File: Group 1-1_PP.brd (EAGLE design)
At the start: 90 x 75 mm, 40 parts, among them IC1 74LS90N, IC10 7805T, IC2 74LS90N, IC3 74LS48N, IC4 74LS48N, IC5 74ALS08N, IC6 LM555N, IC7 74LS14N, IC8 7476N, IC9 74LS32N

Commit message: MANAAAAAAAAAAAAAAAAAAAA
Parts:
- moved C5 146.4 mm to (77.0, 18.7)
- moved C3 144.2 mm to (82.5, 23.7)
- moved C2 131.8 mm to (77.0, 23.7)
- moved IC9 130.4 mm to (60.0, 9.00)
- moved C1 112.7 mm to (82.0, 18.6)
- moved IC7 107.5 mm to (63.0, 34.0)
- moved IC6 105.5 mm to (80.0, 34.0)
- moved IC2 100.7 mm to (30.0, 9.00)
- moved R11 92.7 mm to (21.9, 52.3)
- moved IC5 89.0 mm to (61.0, 21.0)
- moved R19 88.4 mm to (10.9, 3.13)
- moved R10 83.6 mm to (21.9, 49.3)
- moved R17 80.2 mm to (10.8, 66.3)
- moved R16 79.7 mm to (20.9, 69.3)
- moved R5 78.1 mm to (9.85, 55.3)
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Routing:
- net VCC: track 0.00 -> 316.4 mm
- net N$4: track 0.00 -> 138.4 mm
- net N$14: track 0.00 -> 121.5 mm
- net TR: track 0.00 -> 108.5 mm
- net N$3: track 0.00 -> 96.2 mm
- net N$7: track 0.00 -> 87.6 mm
- net CLK_1HZ: track 0.00 -> 84.8 mm
- net N$21: track 0.00 -> 79.5 mm
- net N$23: track 0.00 -> 70.8 mm
- net N$22: track 0.00 -> 69.7 mm
- net RESET: track 0.00 -> 57.9 mm
- net N$5: track 0.00 -> 57.0 mm
- net STRST: track 0.00 -> 56.5 mm
- net N$30: track 0.00 -> 56.0 mm
- net N$1: track 0.00 -> 51.3 mm
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- added copper zone on layer 1, net GND
- added copper zone on layer 16, net GND
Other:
- board text added: "60-second Timer Circuit Rev 1.0"
- board text added: "RESET"
- board text added: "START/STOP"

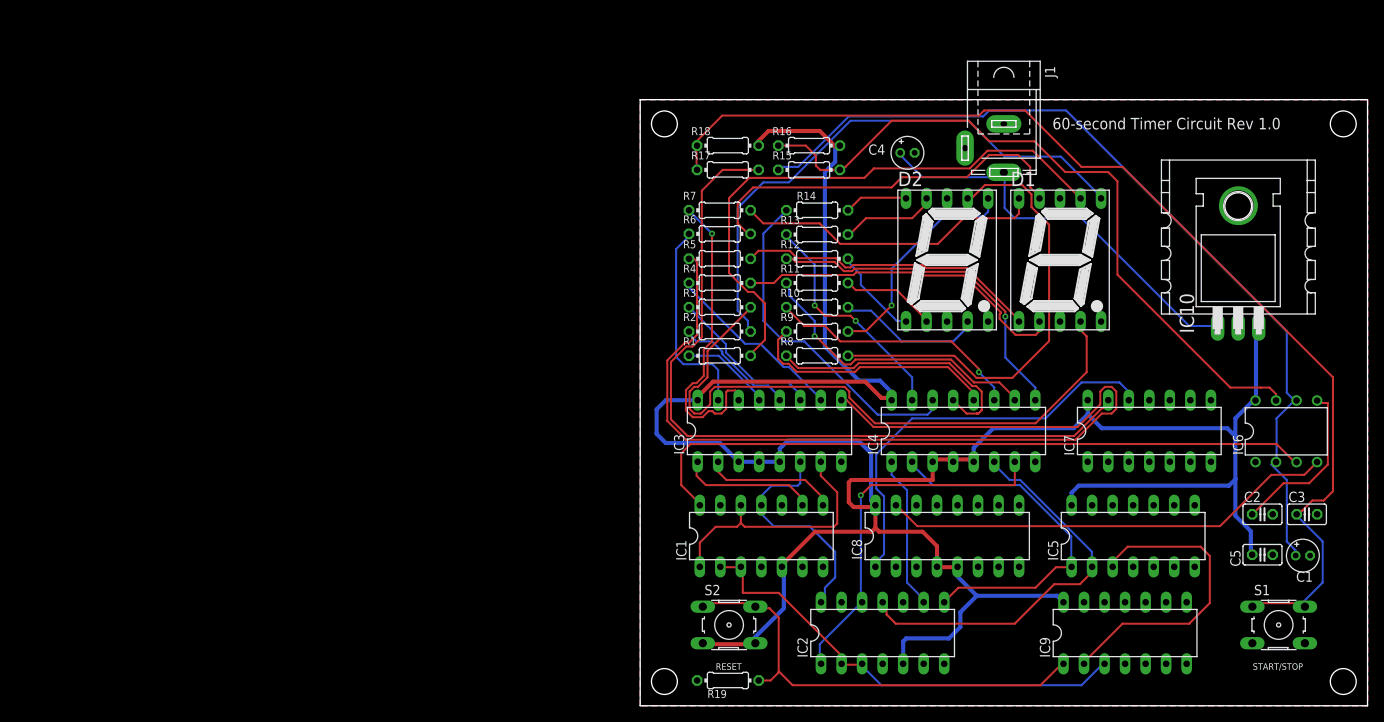
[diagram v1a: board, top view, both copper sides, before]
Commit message: [Zach] Updated lbrs for regulator visibility
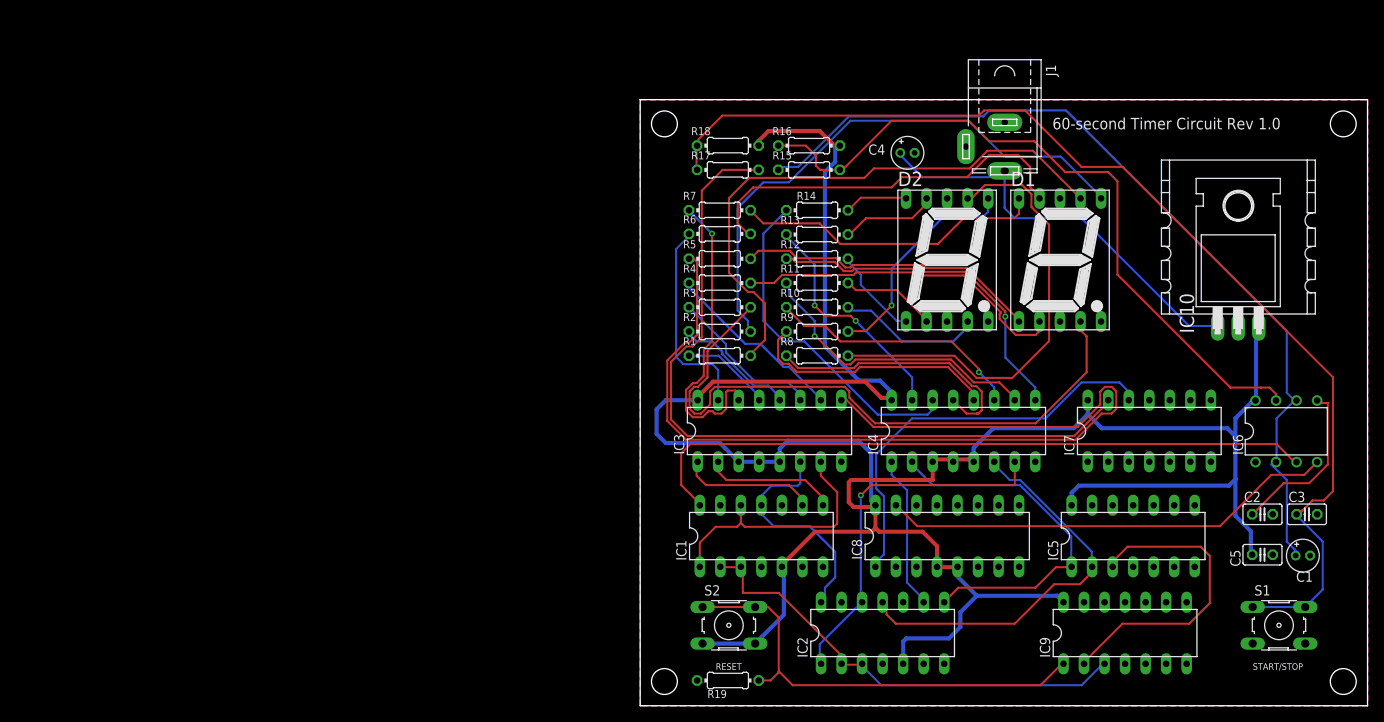
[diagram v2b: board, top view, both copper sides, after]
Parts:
- moved J1 0.22 mm to (45.1, 69.2)
- moved S1 0.06 mm to (79.0, 9.96)
- moved S2 0.05 mm to (11.0, 9.96)
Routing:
- net N$4: track 138.4 -> 137.7 mm

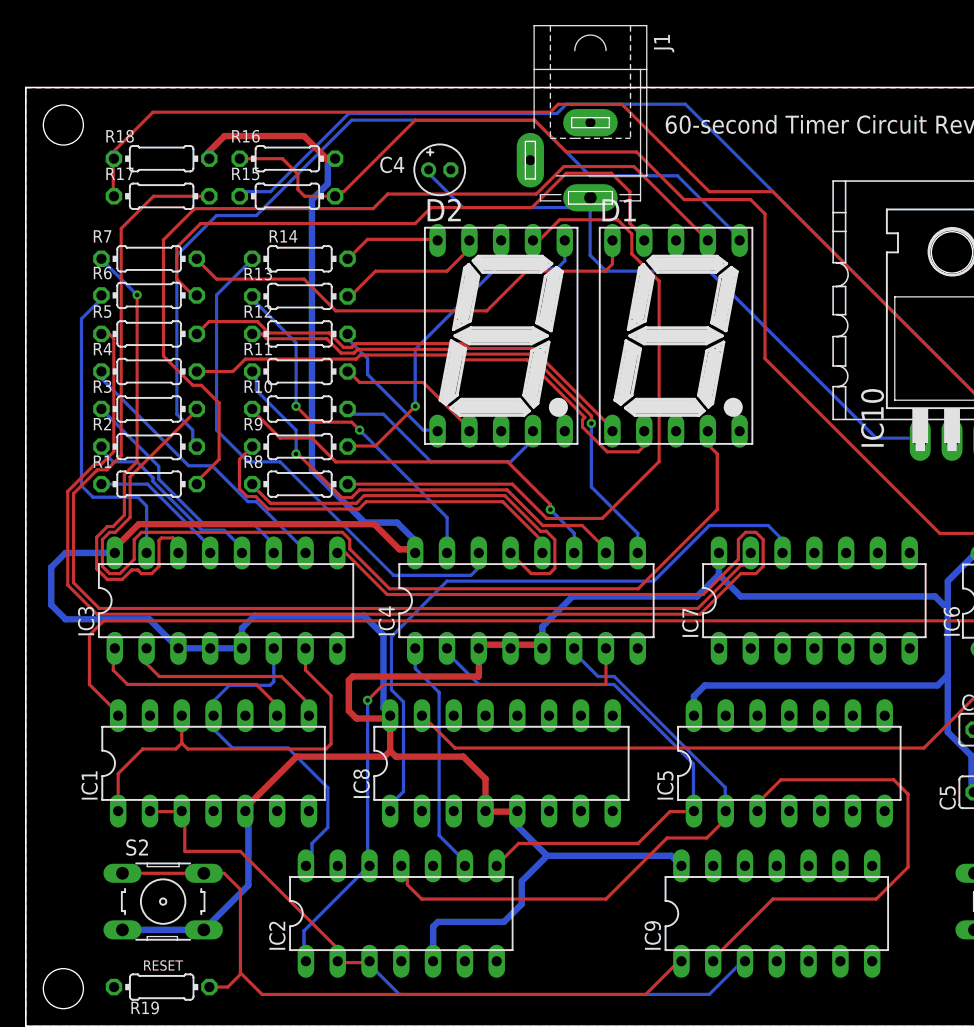
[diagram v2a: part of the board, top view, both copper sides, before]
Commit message: [Zach] Rearranged IC labels
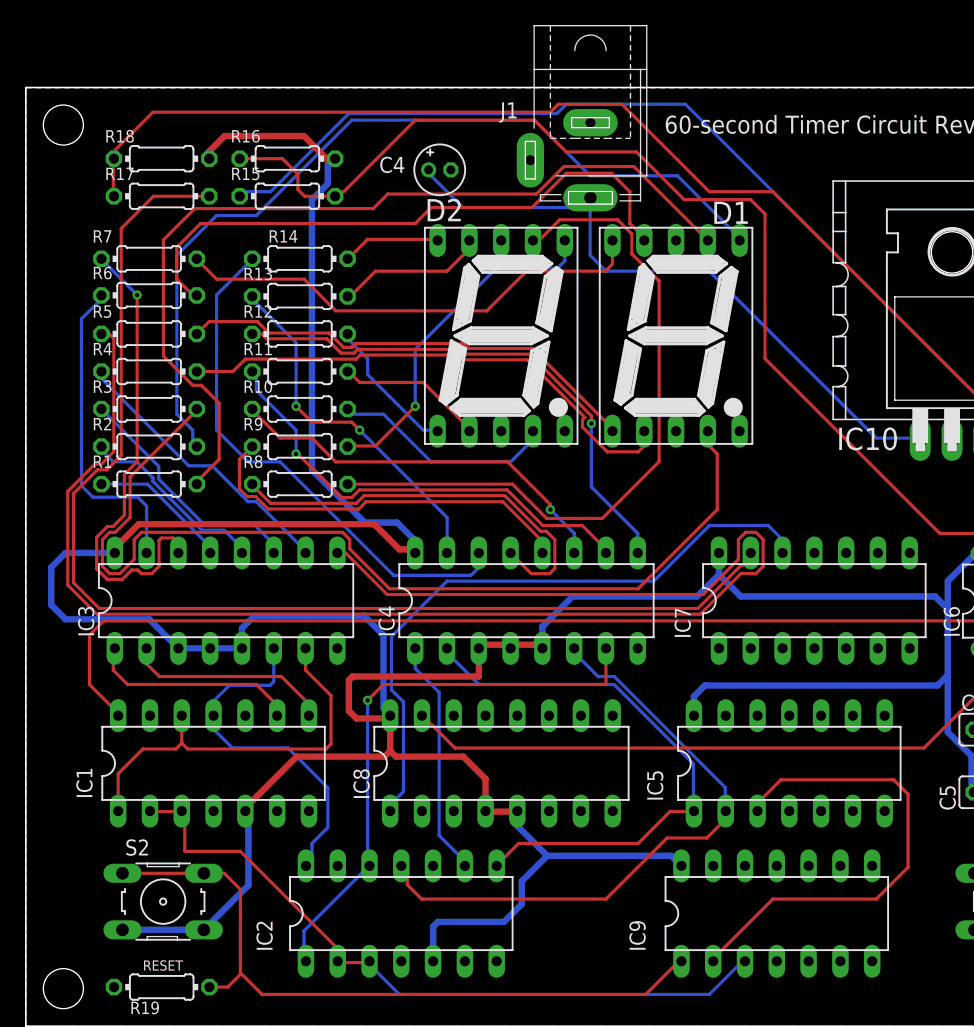
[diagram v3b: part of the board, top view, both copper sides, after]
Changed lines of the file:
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@@
 </layers>
 <board>
-<fusionsync huburn="a.YnVzaW5lc3M6bXl1c2MyMDM5" projecturn="a.YnVzaW5lc3M6bXl1c2MyMDM5I0QyMDIzMDcxNzY1NTg3ODQzMQ" f3durn="urn:adsk.wipprod:dm.lineage:W1NGV9-mTa-5apBo6xWiiA" pcbguid="" lastpulledtime="" lastsyncedchangeguid="" latestrevisionid="328fced8-3078-4b6d-ae1e-fadf76d95870" lastsyncedrevisionid="328fced8-3078-4b6d-ae1e-fadf76d95870" lastboardhashguid="aa4f0186-8a9e-9393-aab9-4abb9243e74a" lastpushedtime="2023-07-21T12:01:13Z" linktopcb3d="true"/>
+<fusionsync huburn="a.YnVzaW5lc3M6bXl1c2MyMDM5" projecturn="a.YnVzaW5lc3M6bXl1c2MyMDM5I0QyMDIzMDcxNzY1NTg3ODQzMQ" f3durn="urn:adsk.wipprod:dm.lineage:W1NGV9-mTa-5apBo6xWiiA" pcbguid="" lastpulledtime="" lastsyncedchangeguid="" latestrevisionid="32b6bed8-b7c8-496e-ad21-02c96e131fee" lastsyncedrevisionid="32b6bed8-b7c8-496e-ad21-02c96e131fee" lastboardhashguid="69073ed8-a101-9280-f158-97f194a30dec" lastpushedtime="2023-07-21T12:26:37Z" linktopcb3d="true"/>
 <plain>
 <wire x1="0" y1="0" x2="0" y2="75" width="0.127" layer="20"/>
@@
 </element>
 <element name="D1" library="special" library_urn="urn:adsk.eagle:library:367" package="7SEG-13" package3d_urn="urn:adsk.eagle:package:26668/2" value="" x="51.95" y="55.16" smashed="yes">
-<attribute name="NAME" x="45.854" y="64.304" size="1.778" layer="25" ratio="10"/>
+<attribute name="NAME" x="54.7948" y="64.1008" size="1.778" layer="25" ratio="10"/>
 <attribute name="POPULARITY" value="3" x="71" y="45" size="1.778" layer="27" display="off"/>
 <attribute name="VALUE" x="45.854" y="44.238" size="1.778" layer="27" ratio="10"/>
@@
 </element>
 <element name="IC1" library="74xx-us" library_urn="urn:adsk.eagle:library:88" package="DIL14" package3d_urn="urn:adsk.eagle:package:16407/2" value="74LS90N" x="15" y="21" smashed="yes">
-<attribute name="NAME" x="5.729" y="17.952" size="1.27" layer="25" ratio="10" rot="R90"/>
+<attribute name="NAME" x="5.3226" y="18.1552" size="1.27" layer="25" ratio="10" rot="R90"/>
 <attribute name="POPULARITY" value="0" x="60.72" y="-18.37" size="1.778" layer="27" display="off"/>
 <attribute name="VALUE" x="8.269" y="20.365" size="1.27" layer="27" ratio="10"/>
 </element>
 <element name="IC2" library="74xx-us" library_urn="urn:adsk.eagle:library:88" package="DIL14" package3d_urn="urn:adsk.eagle:package:16407/2" value="74LS90N" x="30" y="9" smashed="yes">
-<attribute name="NAME" x="20.729" y="5.952" size="1.27" layer="25" ratio="10" rot="R90"/>
+<attribute name="NAME" x="19.713" y="5.952" size="1.27" layer="25" ratio="10" rot="R90"/>
 <attribute name="POPULARITY" value="0" x="96.04" y="-30.37" size="1.778" layer="27" display="off"/>
 <attribute name="VALUE" x="23.269" y="8.365" size="1.27" layer="27" ratio="10"/>
@@
 </element>
 <element name="IC5" library="74xx-us" library_urn="urn:adsk.eagle:library:88" package="DIL14" package3d_urn="urn:adsk.eagle:package:16407/2" value="74ALS08N" x="61" y="21" smashed="yes">
-<attribute name="NAME" x="51.729" y="17.952" size="1.27" layer="25" ratio="10" rot="R90"/>
+<attribute name="NAME" x="50.9162" y="17.952" size="1.27" layer="25" ratio="10" rot="R90"/>
 <attribute name="POPULARITY" value="0" x="83.86" y="-29.8" size="1.778" layer="27" display="off"/>
 <attribute name="VALUE" x="54.269" y="20.365" size="1.27" layer="27" ratio="10"/>
@@
 </element>
 <element name="IC7" library="74xx-us" library_urn="urn:adsk.eagle:library:88" package="DIL14" package3d_urn="urn:adsk.eagle:package:16407/2" value="74LS14N" x="63" y="34" smashed="yes">
-<attribute name="NAME" x="53.729" y="30.952" size="1.27" layer="25" ratio="10" rot="R90"/>
+<attribute name="NAME" x="53.1194" y="30.952" size="1.27" layer="25" ratio="10" rot="R90"/>
 <attribute name="POPULARITY" value="0" x="106.18" y="-16.8" size="1.778" layer="27" display="off"/>
 <attribute name="VALUE" x="56.269" y="33.365" size="1.27" layer="27" ratio="10"/>
@@
 </element>
 <element name="IC9" library="74xx-us" library_urn="urn:adsk.eagle:library:88" package="DIL14" package3d_urn="urn:adsk.eagle:package:16407/2" value="74LS32N" x="60" y="9" smashed="yes">
-<attribute name="NAME" x="50.729" y="5.952" size="1.27" layer="25" ratio="10" rot="R90"/>
+<attribute name="NAME" x="49.5098" y="5.952" size="1.27" layer="25" ratio="10" rot="R90"/>
 <attribute name="POPULARITY" value="9" x="123.5" y="-41.8" size="1.778" layer="27" display="off"/>
 <attribute name="VALUE" x="53.269" y="8.365" size="1.27" layer="27" ratio="10"/>
@@
 <attribute name="VALUE" x="20.2744" y="45.8274" size="0.9906" layer="27" ratio="10"/>
 </element>
-<element name="IC10" library="linear" package="TO220H" package3d_urn="urn:adsk.eagle:package:41056971/3" value="7805T" x="74" y="57" smashed="yes">
-<attribute name="NAME" x="68.539" y="46.078" size="1.778" layer="25" ratio="10" rot="R90"/>
+<element name="IC10" library="linear" package="TO220H" package3d_urn="urn:adsk.eagle:package:41056971/4" value="7805T" x="74" y="57" smashed="yes">
+<attribute name="NAME" x="69.746" y="47.8126" size="1.778" layer="25" ratio="10" rot="R180"/>
 <attribute name="POPULARITY" value="35" x="74" y="57" size="1.778" layer="27" display="off"/>
-<attribute name="VALUE" x="81.366" y="45.951" size="1.778" layer="27" ratio="10" rot="R90"/>
+<attribute name="VALUE" x="84.9098" y="47.838" size="1.778" layer="27" ratio="10" rot="R180"/>
 </element>
 <element name="HS1" library="to220-heatsink" library_urn="urn:adsk.eagle:library:41058283" package="TO-220H" package3d_urn="urn:adsk.eagle:package:41058286/12" value="507302B00000G" x="64.5" y="58" smashed="yes" rot="R270"/>
@@
 <attribute name="MF" value="" x="45.1104" y="69.1896" size="1.778" layer="27" rot="R270" display="off"/>
 <attribute name="MPN" value="" x="45.1104" y="69.1896" size="1.778" layer="27" rot="R270" display="off"/>
-<attribute name="NAME" x="50.1904" y="79.3496" size="1.27" layer="25" rot="R270"/>
+<attribute name="NAME" x="37.8968" y="72.5424" size="1.27" layer="25"/>
 <attribute name="OC_FARNELL" value="unknown" x="45.1104" y="69.1896" size="1.778" layer="27" rot="R270" display="off"/>
 <attribute name="OC_NEWARK" value="unknown" x="45.1104" y="69.1896" size="1.778" layer="27" rot="R270" display="off"/>
@@
 <contactref element="J1" pad="1"/>
 <contactref element="J1" pad="2"/>
-<wire x1="40.3104" y1="69.1896" x2="45.1104" y2="72.1896" width="0" layer="19" extent="1-1"/>
-<wire x1="7.0468" y1="3.1276" x2="45.1104" y2="72.1896" width="0" layer="19" extent="1-1"/>
 </signal>
 <signal name="VCC">

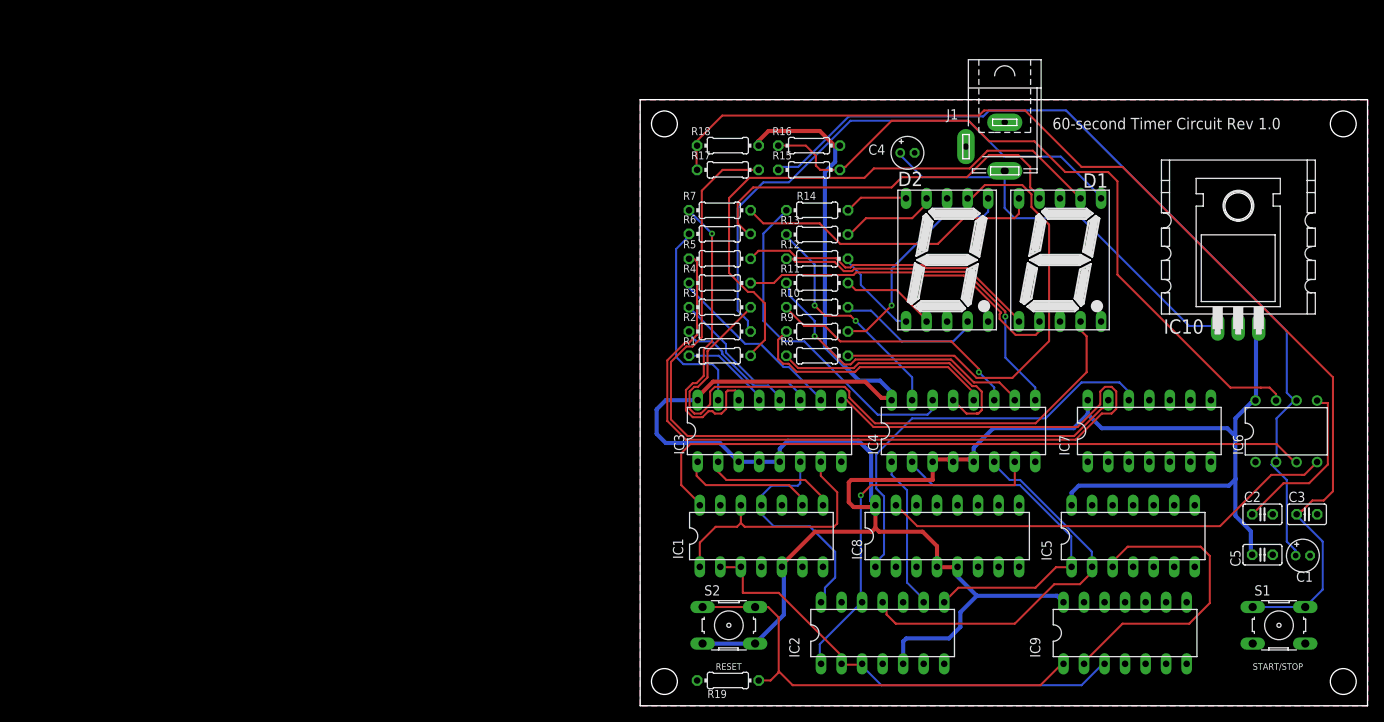
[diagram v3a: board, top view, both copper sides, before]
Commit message: [Zach] Changed track widths
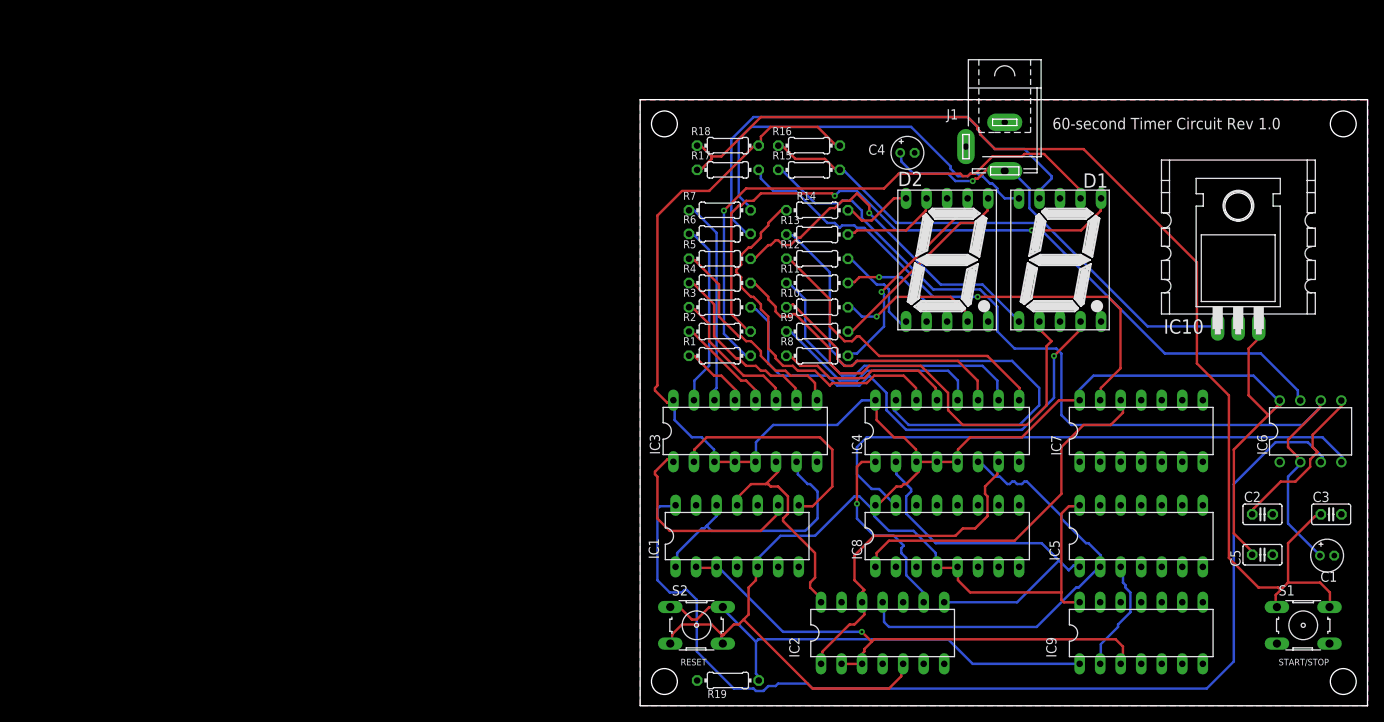
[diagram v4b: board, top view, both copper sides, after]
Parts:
- moved S2 4.00 mm to (6.97, 9.96)
- moved C1 3.00 mm to (85.0, 18.6)
- moved C3 3.00 mm to (85.5, 23.7)
- moved IC1 3.00 mm to (12.0, 21.0)
- moved IC3 3.00 mm to (13.0, 34.0)
- moved IC6 3.00 mm to (83.0, 34.0)
- moved S1 3.00 mm to (82.0, 9.96)
- moved IC4 2.00 mm to (38.0, 34.0)
- moved IC9 2.00 mm to (62.0, 9.00)
- moved IC5 1.00 mm to (62.0, 21.0)
- moved IC7 1.00 mm to (62.0, 34.0)
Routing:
- net N$14: track 121.5 -> 26.9 mm
- net CLK_1HZ: track 84.8 -> 130.9 mm
- net N$28: track 28.8 -> 68.7 mm, vias 2 -> 0
- net N$3: track 96.2 -> 65.0 mm, vias 0 -> 1
- net N$30: track 56.0 -> 26.4 mm, vias 0 -> 1
- net CNT_6: track 38.5 -> 14.1 mm
- net N$20: track 41.6 -> 60.1 mm
- net N$21: track 79.5 -> 61.6 mm, vias 0 -> 1
- net STRST: track 56.5 -> 72.0 mm
- net N$10: track 16.5 -> 29.6 mm
- net N$16: track 38.2 -> 25.4 mm, vias 1 -> 0
- net F1: track 48.4 -> 60.6 mm
- net G1: track 38.4 -> 49.0 mm
- net N$17: track 33.3 -> 22.7 mm
- net N$8: track 17.0 -> 26.5 mm
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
